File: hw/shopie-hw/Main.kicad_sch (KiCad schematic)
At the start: 46 parts, among them J1 Jack-DC, J2 USB_B_Micro, J3 Conn_01x04_Socket, SW1 SW_SPDT, SW2 SW_MEC_5E, SW3 SW_SPDT, U2 STM32F405RGT6, U3 LM2596T-5, U4 AP2112K-3.3, U6 MIC5365-1.8YC5, U9 LTC2943, Y2 Crystal_Small

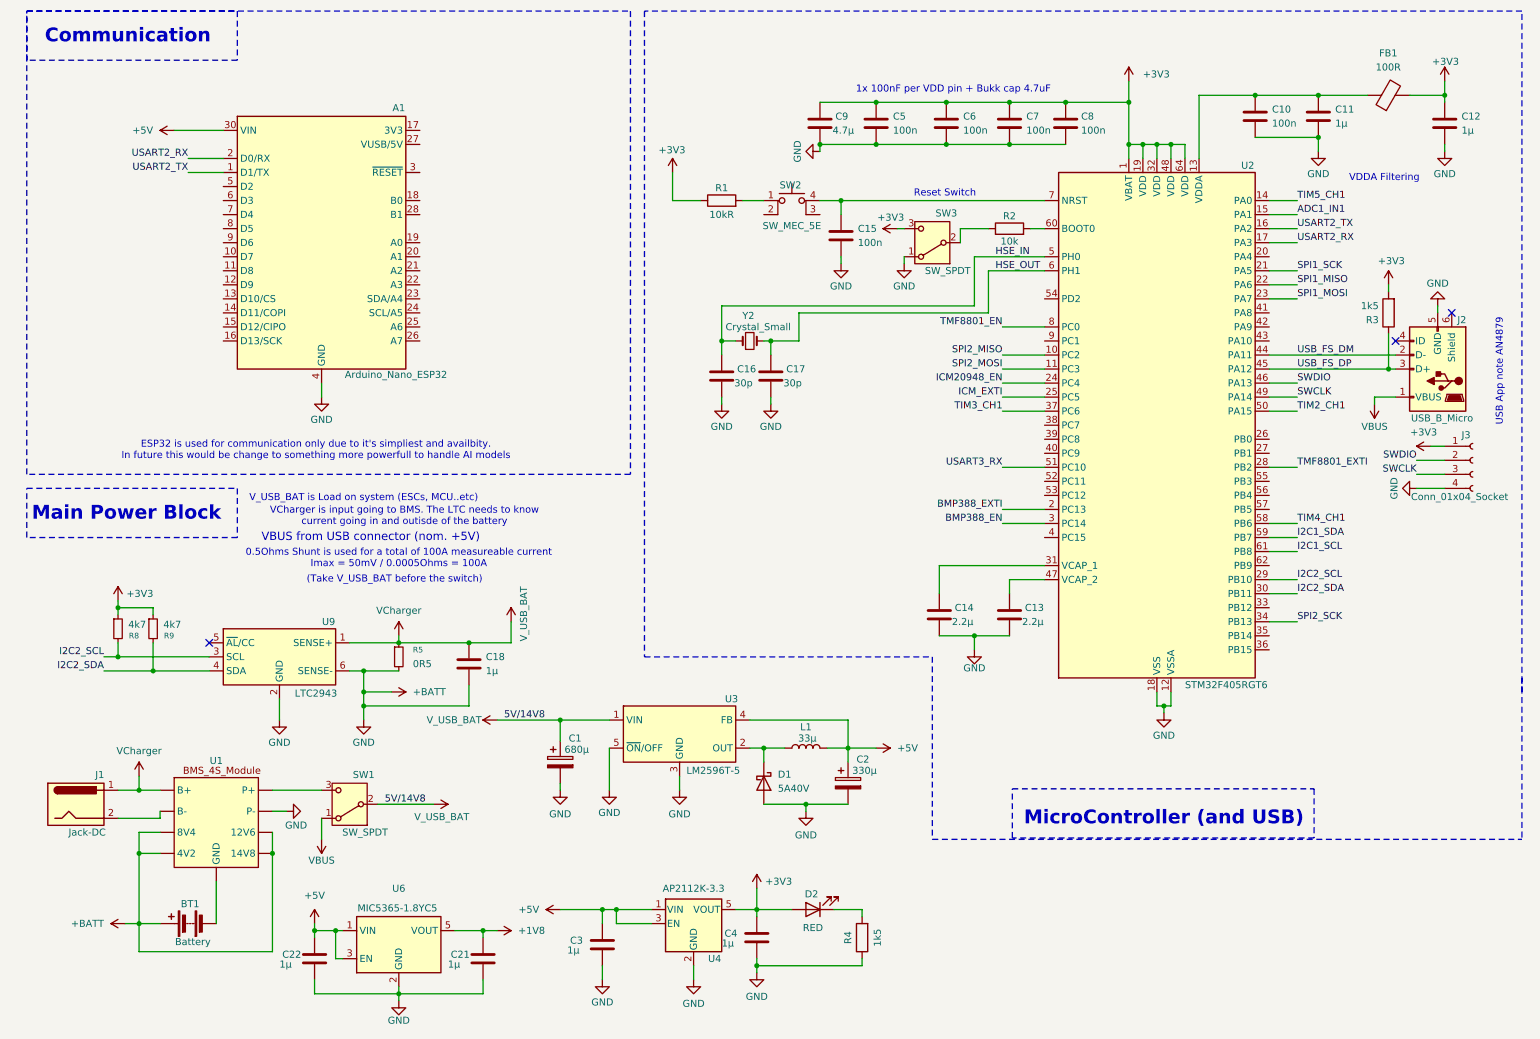
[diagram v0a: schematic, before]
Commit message: Add custom footprint for BMS board, Add TMF8801 footprint
- Created custom footprint for the BMS board
- Imported TMF8801 sensor footprint
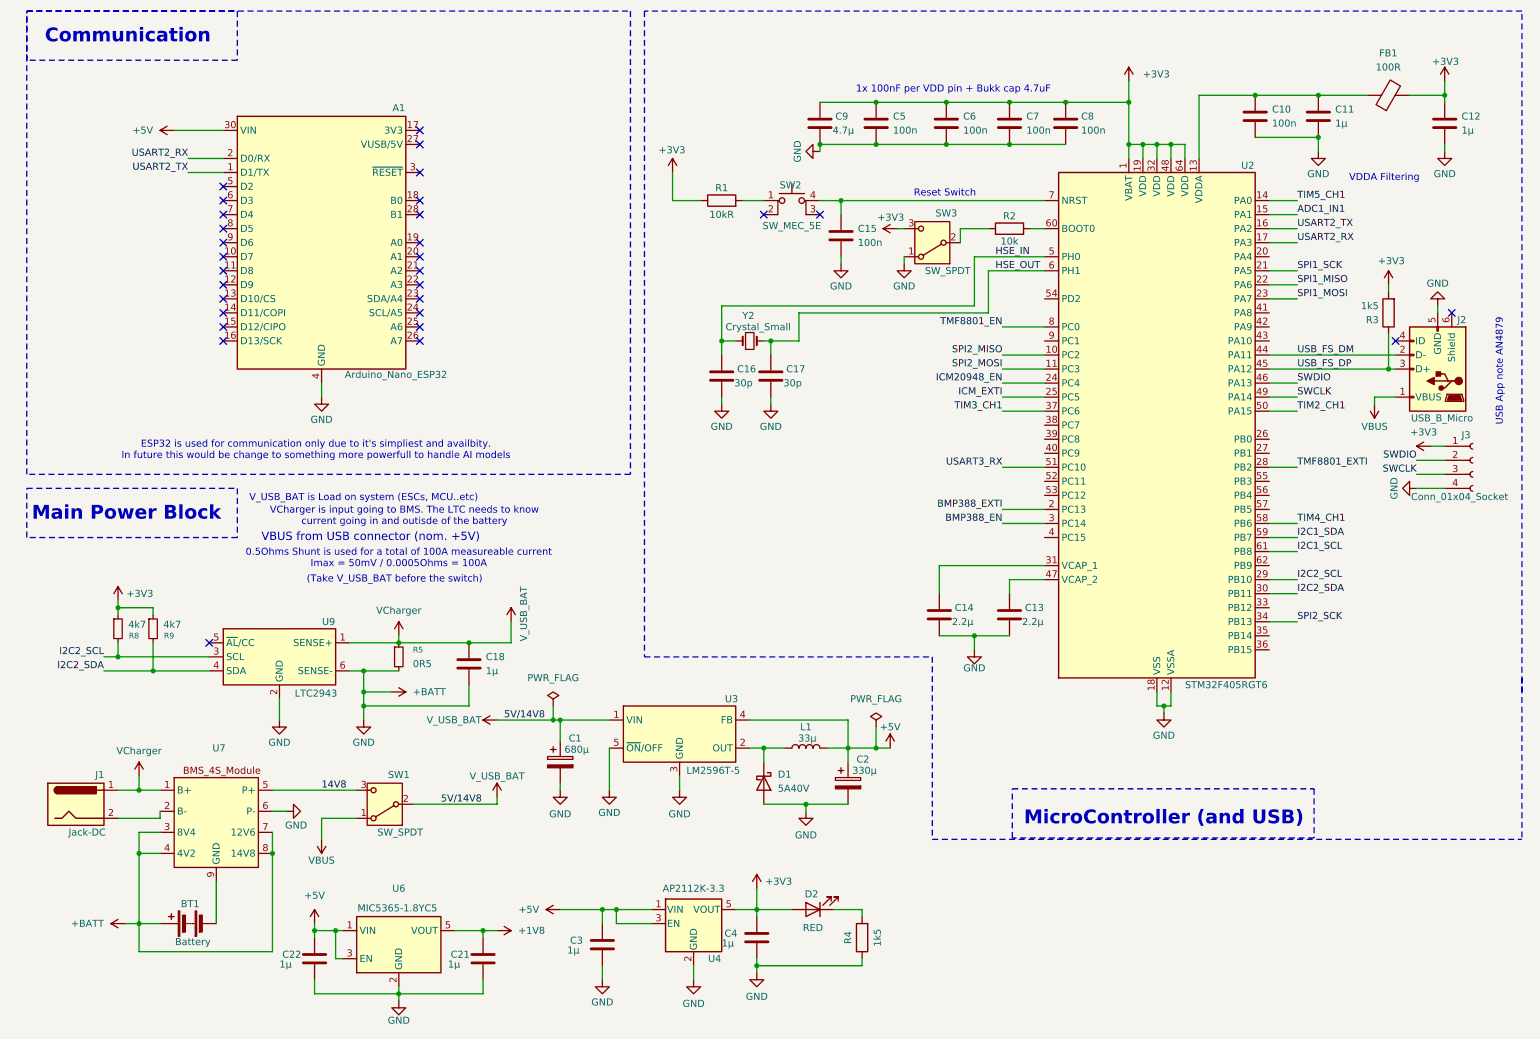
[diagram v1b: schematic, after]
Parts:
- removed U1: ~, symbol shopie-hwLibrary:BMS_4S_Module
- added U7: ~, symbol shopie-hwLibrary:BMS_4S_Module
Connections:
- net +BATT: now also U7.3 (8V4), U7.4 (4V2), U7.6 (P-), U7.7 (12V6), U7.8 (14V8)
- net VCharger: now also U7.1 (B+)
- net at J1.2: now also U7.2 (B-)
- net 14V8: now reaches SW1.3 (C)
- net 14V8: now also U7.5 (P+)
- net at BT1.2 (-): now also U7.9 (GND)
- no-connect marks 3 -> 30
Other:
- moved on the sheet: SW1

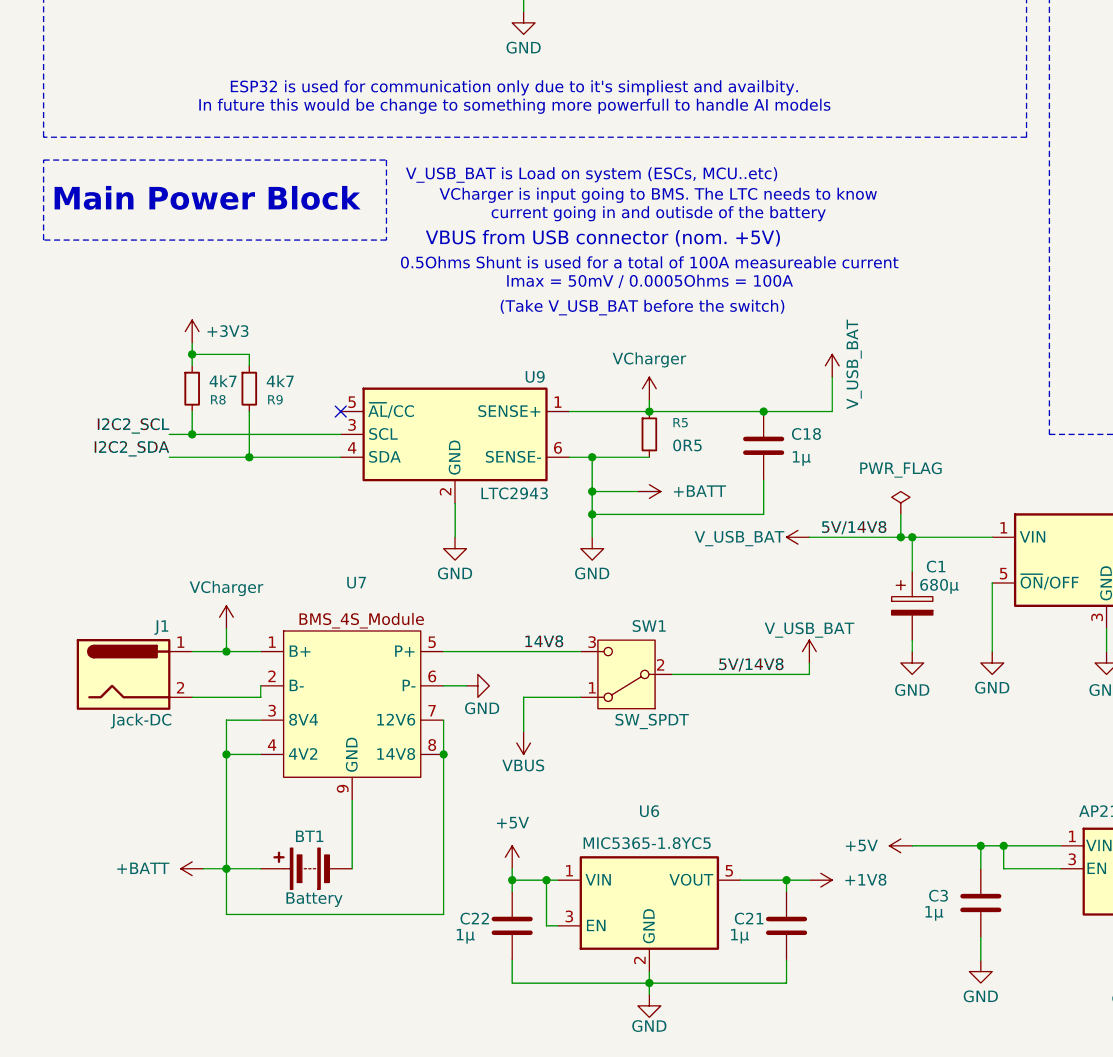
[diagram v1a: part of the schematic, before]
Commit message: Update BMS Module Symbol
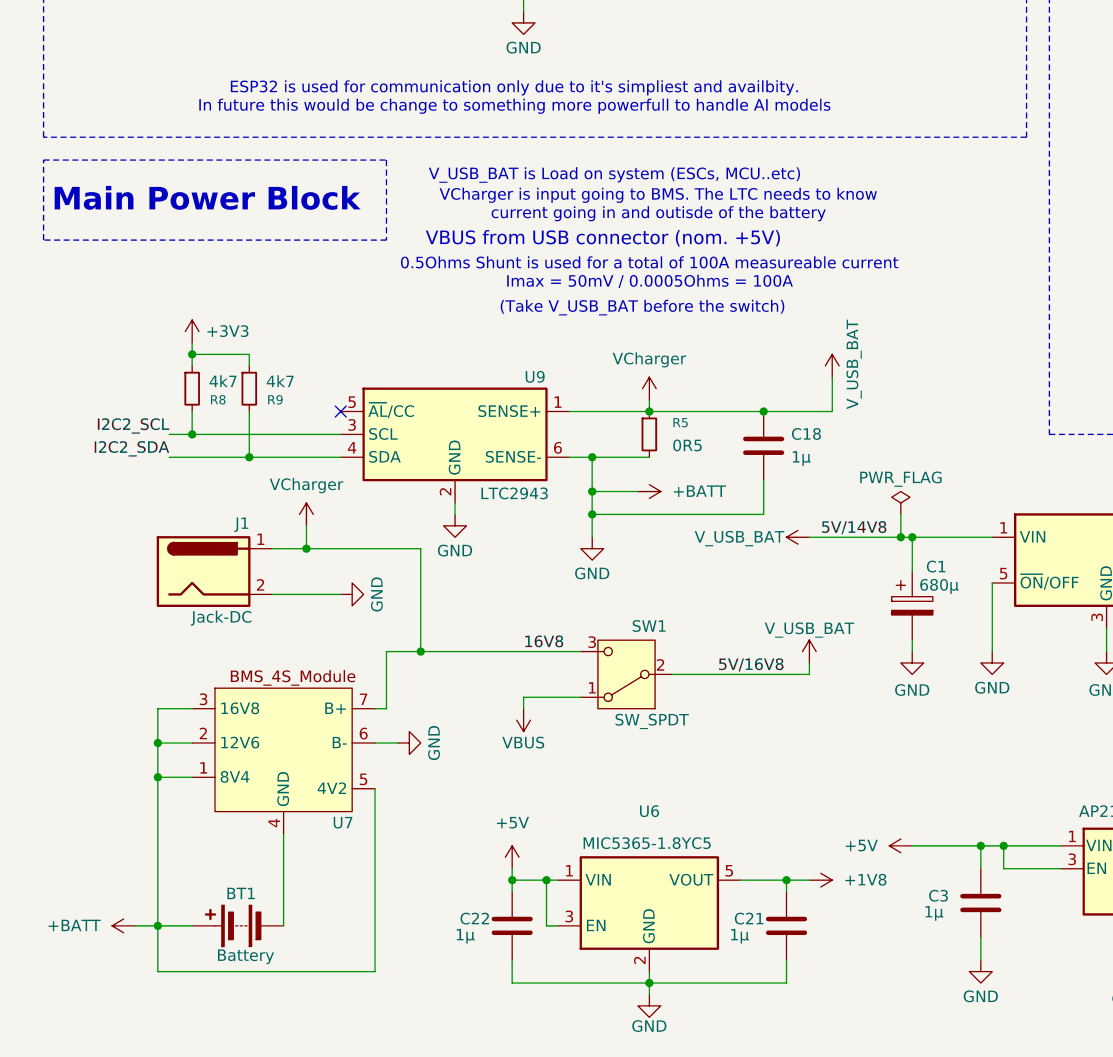
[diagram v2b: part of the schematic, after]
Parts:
- U7: footprint (none) -> ShopieLibrary:BMS_4S_40A
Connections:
- net +BATT: now also J1.2, U7.1 (8V4), U7.2 (12V6), U7.5 (4V2); no longer U7.4 (4V2), U7.7 (12V6), U7.8 (14V8)
- net VCharger: now also SW1.3 (C), U7.7 (B+); no longer U7.1 (B+)
- net at BT1.2 (-): now also U7.4 (GND); no longer U7.9 (GND)
- removed net 14V8: SW1.3 (C), U7.5 (P+)
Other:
- moved on the sheet: BT1, J1

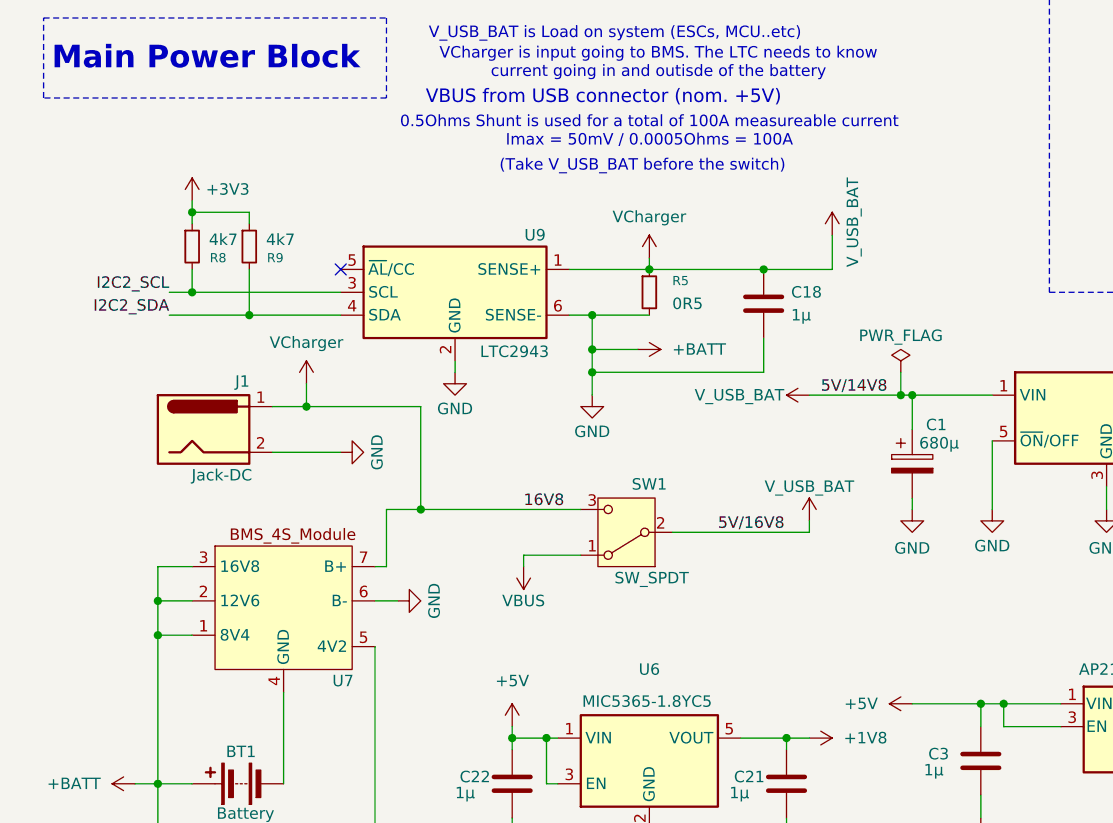
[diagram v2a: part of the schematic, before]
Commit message: Update Main Power Block
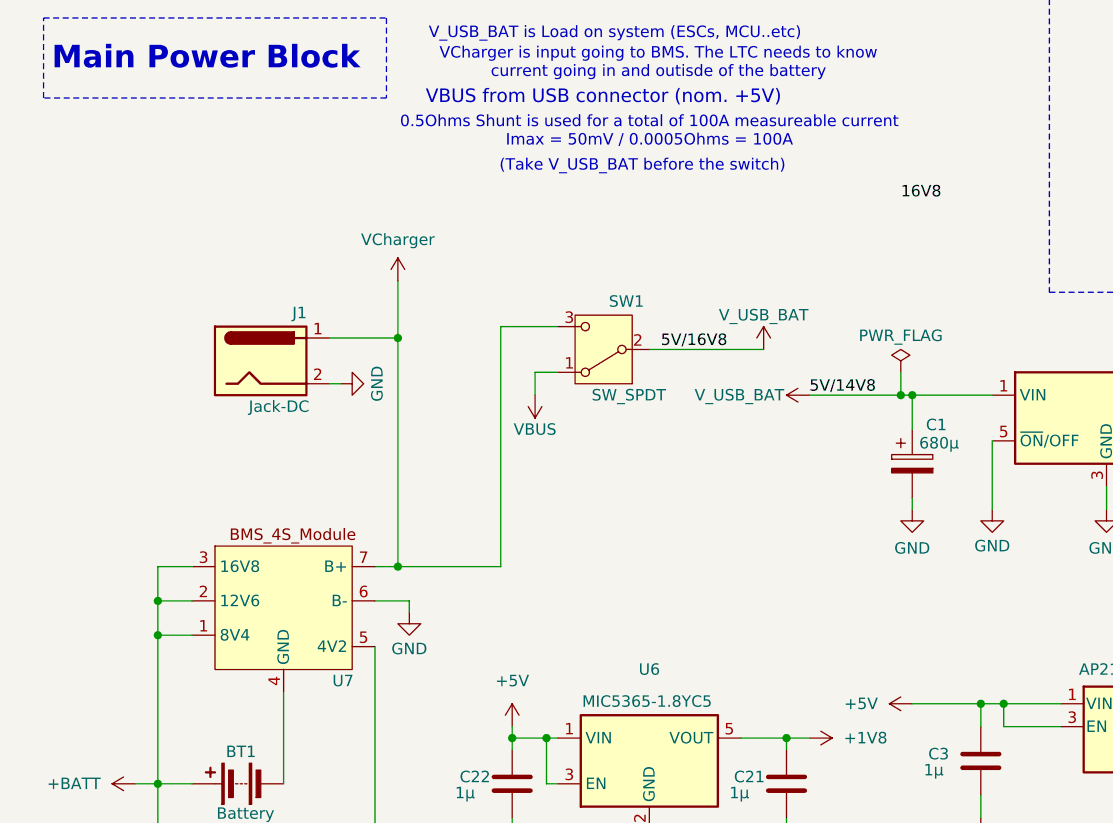
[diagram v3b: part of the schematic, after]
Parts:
- removed C18: 1µ, symbol Device:C
- removed R5: 0R5, symbol Device:R_Small
- removed R8, R9: 4k7, symbol Device:R_Small
- removed U9: LTC2943, Package_DFN_QFN:DFN-6-1EP_3x2mm_P0.5mm_EP1.65x1.35mm, symbol Battery_Management:LTC2942
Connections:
- net +BATT: no longer A1.29 (GND), A1.4 (GND), C1.2, C10.2, C11.2, C12.2, C13.2, C14.2, C15.2, C16.2, C17.2, C2.2, C21.2, C22.2, C3.2, C4.2, C5.2, C6.2, C7.2, C8.2, C9.2, D1.2 (A), J1.2, J2.5 (GND), J3.4 (Pin_4), R4.1, SW3.1 (A), U2.12 (VSSA), U2.18 (VSS), U2.63 (VSS), U3.3 (GND), U3.5 (~{ON}/OFF), U4.2 (GND), U6.2 (GND), U7.6 (B-)
- net VCharger: no longer C1.1, SW1.2 (B), U3.1 (VIN)
- new net GND: A1.29 (GND), A1.4 (GND), C1.2, C10.2, C11.2, C12.2, C13.2, C14.2, C15.2, C16.2, C17.2, C2.2, C21.2, C22.2, C3.2, C4.2, C5.2, C6.2, C7.2, C8.2, C9.2, D1.2 (A), J1.2, J2.5 (GND), J3.4 (Pin_4), R4.1, SW3.1 (A), U2.12 (VSSA), U2.18 (VSS), U2.63 (VSS), U3.3 (GND), U3.5 (~{ON}/OFF), U4.2 (GND), U6.2 (GND), U7.6 (B-)
- new net V_USB_BAT: C1.1, SW1.2 (B), U3.1 (VIN)
- no-connect marks 30 -> 29
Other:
- moved on the sheet: J1, SW1

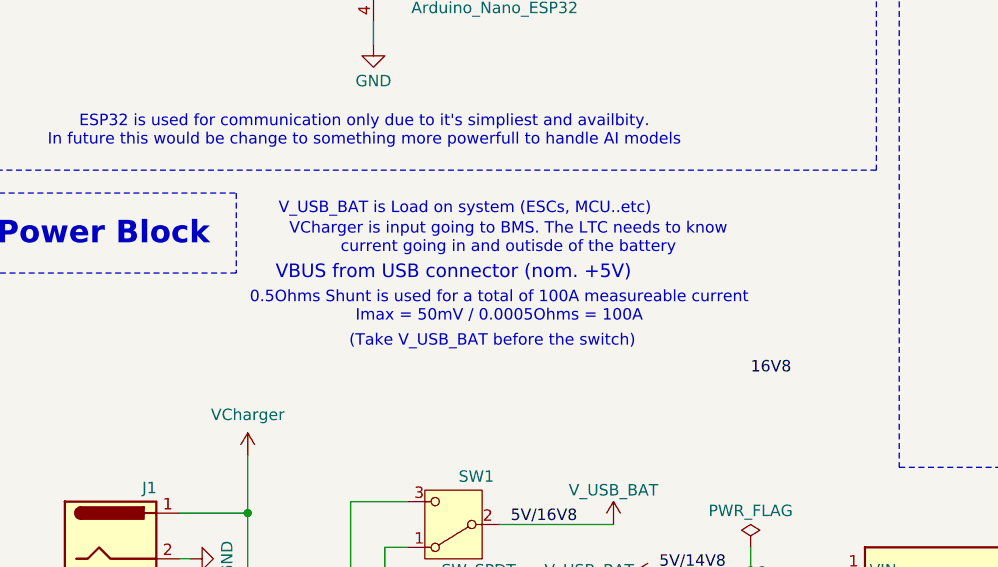
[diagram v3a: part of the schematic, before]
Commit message: Add BSC016N06NS Symbol and Footprint
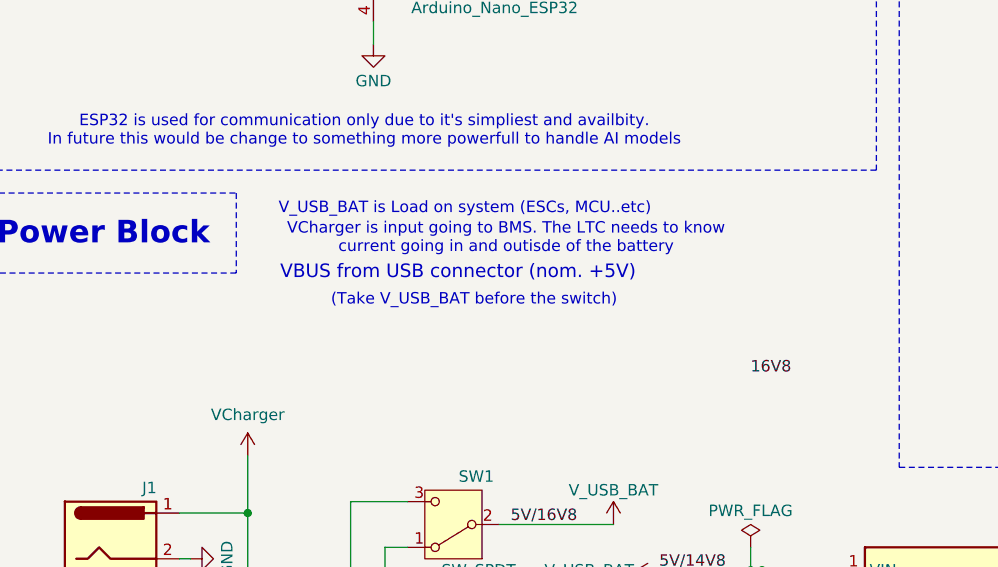
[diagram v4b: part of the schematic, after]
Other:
- note removed: "0.5Ohms Shunt is used for a total of 100A measureable current Imax = 50mV / 0.0005Ohms = 100A"
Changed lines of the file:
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@@
 	(text "VCharger is input going to BMS. The LTC needs to know \ncurrent going in and outisde of the battery\n"
 		(exclude_from_sim no)
-		(at 81.026 104.14 0)
+		(at 80.772 104.14 0)
 		(effects
 			(font
@@
 		)
 	)
-	(text "0.5Ohms Shunt is used for a total of 100A measureable current\nImax = 50mV / 0.0005Ohms = 100A"
-		(exclude_from_sim no)
-		(at 80.01 111.76 0)
-		(effects
-			(font
-				(size 1.27 1.27)
-			)
-		)
-	)
 	(text "USB App note AN4879\n"
 		(exclude_from_sim no)
@@
 	(text "(Take V_USB_BAT before the switch)"
 		(exclude_from_sim no)
-		(at 79.248 115.57 0)
+		(at 77.216 110.998 0)
 		(effects
 			(font
@@
 	(text "VBUS from USB connector (nom. +5V) "
 		(exclude_from_sim no)
-		(at 74.93 107.95 0)
+		(at 75.438 107.95 0)
 		(effects
 			(font
